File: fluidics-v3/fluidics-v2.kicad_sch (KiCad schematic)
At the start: 35 parts, among them J1 PJ-063AH, J10 87832-0410, J11 0705430001, J12 87832-0410, J13 0705430001, J14 87832-0410, J15 0533980671, J16 0705430001, J17 0533980671, J18 87832-0410, J19 0705430001, J2 B6B-ZR-SM4-TF, J20 0533980671, J21 87832-0410, J22 0705430001, J24 0705430001, J25 87832-0410, J3 A-DS_15_A_KG-T4S, J4 B6B-ZR-SM4-TF, U2 Teensy4.1

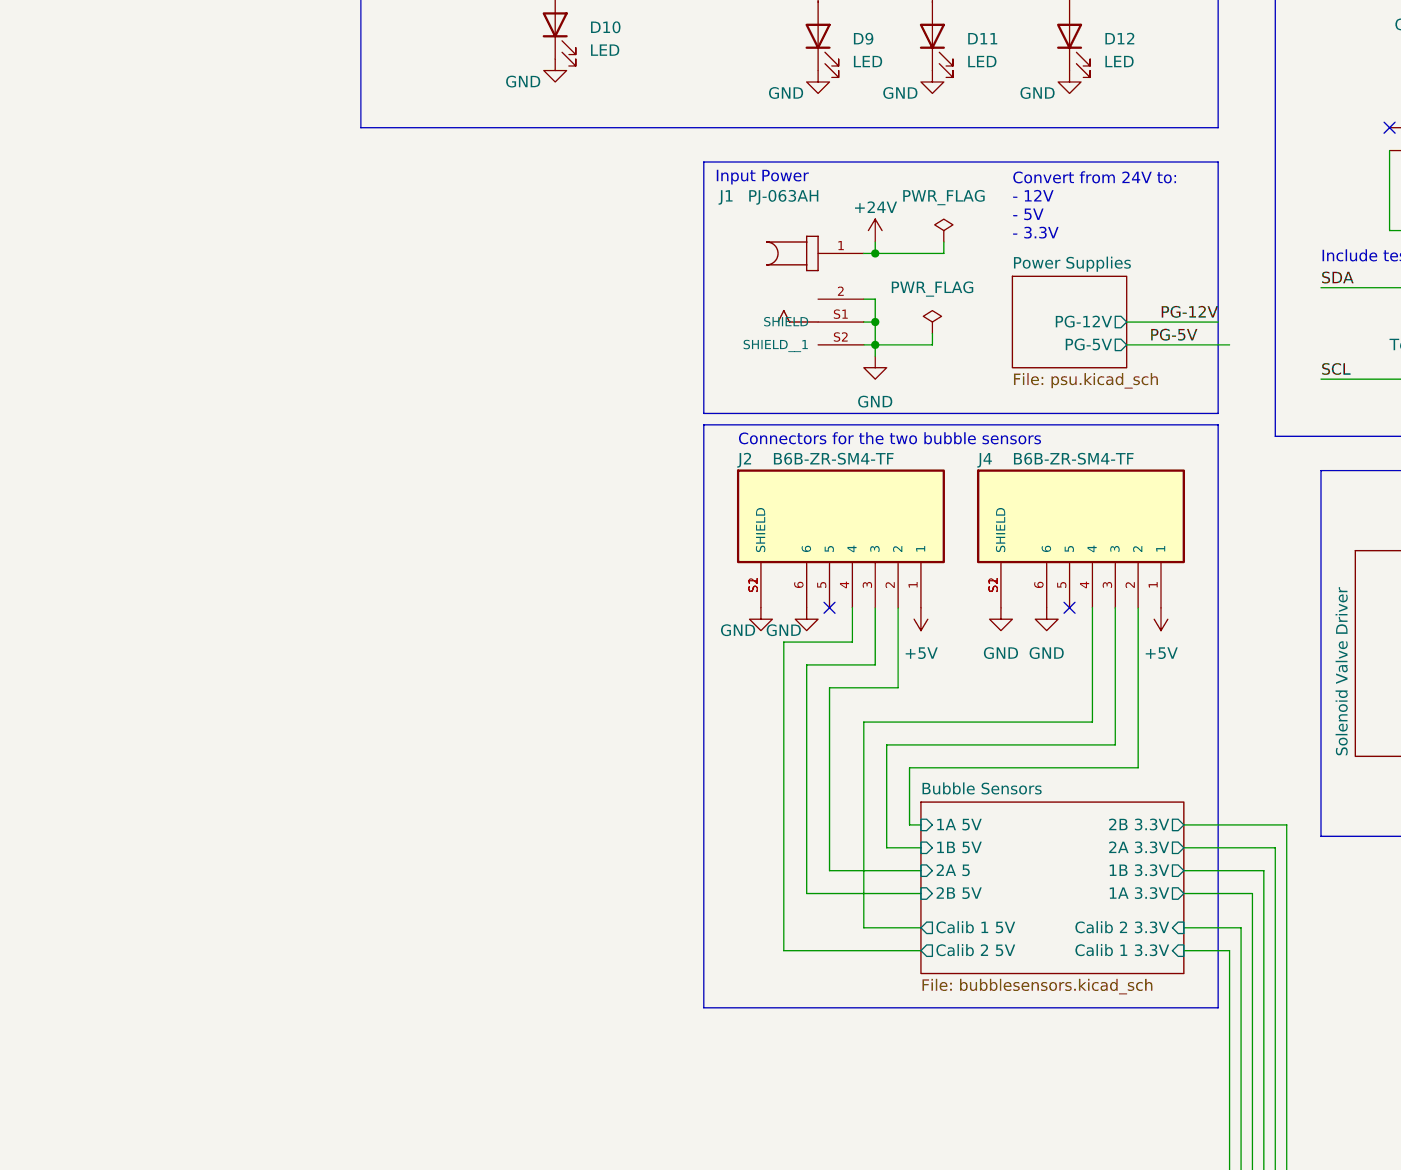
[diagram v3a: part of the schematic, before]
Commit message: v3 PCB: complete +24V input-protection front-end + downsize bulk caps
Input stage (J1 barrel jack -> TH1 NTC inrush limiter -> +24V plane):
- Fix +24V-into-J1 short + solder-mask bridge (leftover rail track ran
  into the /+24V_IN pad after J1 was repurposed as the input)
- Tie in U6.5 GND and C3 +24V bulk cap; stitch 3 isolated GND pour islands
- Route /+24V_IN on Front at 1.5mm (carries full board +24V current)

Bulk caps downsized, capacitance unchanged, all re-tied via-to-plane:
- C3  100uF/+24V: electrolytic CP_Elec_8x10.5 -> polymer CP_EIA-7343-20 (~2mm)
- C4   47uF/+3V3: electrolytic -> C_1206 ceramic
- C10 100uF/+5V:  electrolytic -> C_1210 ceramic
Schematic footprints updated to match (schematic/PCB parity clean).

DRC: 0 shorts/clearance/hole/isolated/parity; 6 unconnected
(5 intentional U2 no-connects + 1 pre-existing +5V stub gap).

Co-Authored-By: Claude Opus 4.8 (1M context) <noreply@anthropic.com>
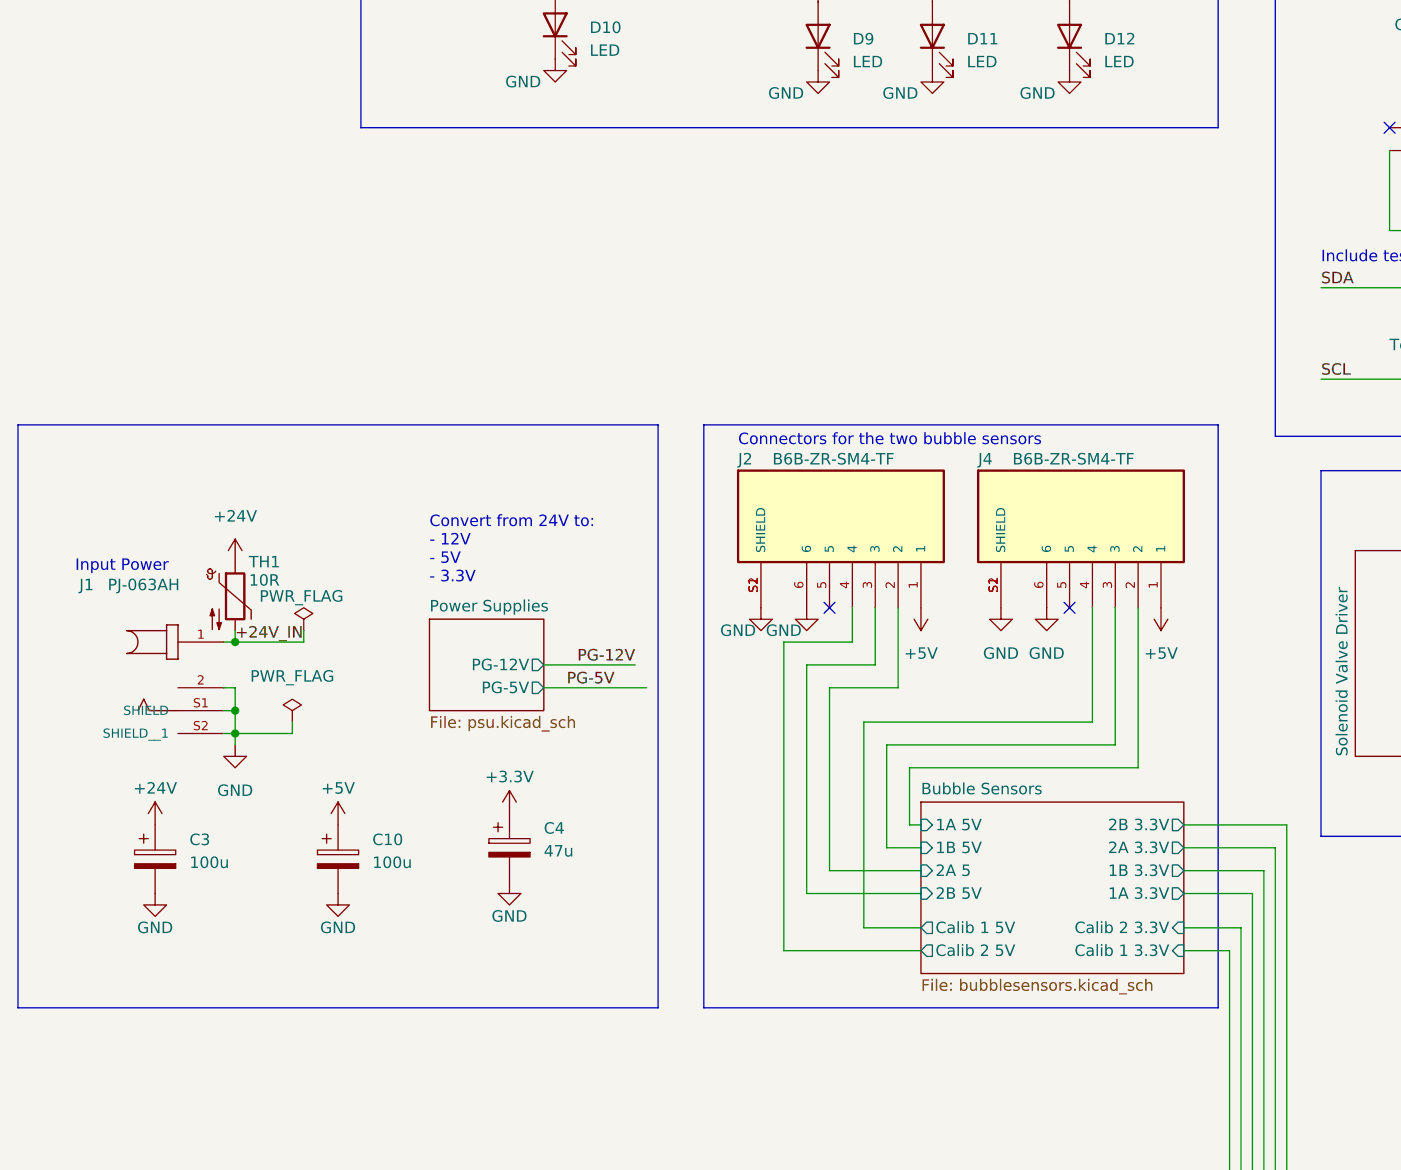
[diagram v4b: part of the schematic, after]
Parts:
- added C10: 100u, Capacitor_SMD:C_1210_3225Metric, symbol Device:C_Polarized
- added C3: 100u, Capacitor_Tantalum_SMD:CP_EIA-7343-20_Kemet-V, symbol Device:C_Polarized
- added C4: 47u, Capacitor_SMD:C_1206_3216Metric, symbol Device:C_Polarized
- added TH1: 10R, Varistor:RV_Disc_D7mm_W3.9mm_P5mm, symbol Device:Thermistor_NTC
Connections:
- net +24V: now also C3.1, TH1.1; no longer J1.1
- net +3.3V: now also C4.1
- net +5V: now also C10.1
- net GND: now also C10.2, C3.2, C4.2
- new net +24V_IN: J1.1, TH1.2
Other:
- moved on the sheet: J1

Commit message: v3: mounting holes M2->M3, relink C3/C4/C10, regen fab package
Mounting holes H2-H4: MountingHole_2.2mm_M2 -> 3.2mm_M3 (PCB + schematic,
parity clean). Note: still 3 holes, no H1 (the original board had 4x M3).

Fix bulk-cap schematic links. C3/C4/C10 had no (path) link to their
symbols and lacked the library prefix in their footprint id, so "Update
PCB from Schematic" deleted and re-added them (losing routing). Relinked:
- C3  Capacitor_Tantalum_SMD:CP_EIA-7343-20_Kemet-V -> /cbfc97bd
- C4  Capacitor_SMD:C_1206_3216Metric              -> /5064b71f
- C10 Capacitor_SMD:C_1210_3225Metric              -> /25d2ffd2

Regenerated fabrication/v3 (gerbers, drill incl. new 3.2mm tool, gerber
zip, STEP, BOM, positions) to reflect the M3 holes.

DRC: 0 clearance/hole/short/isolated, 0 schematic-parity. Remaining are
pre-existing: 24 malformed_courtyard on U2 (footprint geometry) and 6
unconnected (5 intentional U2 no-connects + 1 +5V stub).

Co-Authored-By: Claude Opus 4.8 (1M context) <noreply@anthropic.com>
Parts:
- H2, H3, H4: footprint MountingHole:MountingHole_2.2mm_M2_Pad_Via -> MountingHole:MountingHole_3.2mm_M3_Pad_Via
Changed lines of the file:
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@@
 			)
 		)
-		(property "Footprint" "MountingHole:MountingHole_2.2mm_M2_Pad_Via"
+		(property "Footprint" "MountingHole:MountingHole_3.2mm_M3_Pad_Via"
 			(at 199.39 261.62 0)
 			(hide yes)
@@
 			)
 		)
-		(property "Footprint" "MountingHole:MountingHole_2.2mm_M2_Pad_Via"
+		(property "Footprint" "MountingHole:MountingHole_3.2mm_M3_Pad_Via"
 			(at 203.2 266.7 0)
 			(hide yes)
@@
 			)
 		)
-		(property "Footprint" "MountingHole:MountingHole_2.2mm_M2_Pad_Via"
+		(property "Footprint" "MountingHole:MountingHole_3.2mm_M3_Pad_Via"
 			(at 199.39 279.4 0)
 			(hide yes)

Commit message: Split Teensy U2 into module + two 1x24 SMT sockets
U2 was one part standing in for three physical items: the Teensy 4.1 module
and the two 24-pin SMT socket strips it plugs into. The sockets existed only
as 3D models -- no refdes, no BOM line, no CPL entry -- so an assembler had
no way to order or place them.

New footprint teensy4.1:PinSocket_1x24_P2.54mm_Vertical_SMD_DualLand: 48 pads,
pin numbers 1-24 doubled, coordinates lifted verbatim from U2's lands. Every
pin has a land on both sides (the union of the Harwin M20-786 pin1-left and
pin1-right tail patterns), so strips fit in either orientation and a row may
be made up from shorter pieces. One footprint serves both sockets -- J7 is J6
rotated 180 degrees, which is why J7 pin n lands on old U2 pin n+24.

Schematic: J6/J7 (Conn_01x24) carry the 48 nets via labels on the root sheet;
GND power symbols on J6.1/J7.10/J7.23; no-connect flags on J6.2/J6.3/J6.15/
J7.22. U2 keeps its symbol and BOM line but is marked exclude-from-board.
Seven nets that had no root-sheet name were named to make the join explicit:
/Bubble Sensors/{2B,2A,1B,1A,Calib 2,Calib 1} 3.3V -> BUB_*, Net-(D21-K) -> VIN.

PCB: J6 at (170.61, 51.33) rot 0, J7 at (185.85, 51.33) rot 180 -- all 96 pads
sit exactly on the coordinates U2's lands occupied, so no copper moved. U2's
footprint removed. Module body added back as documentation: 61.0 x 17.78 mm
outline plus "U2 Teensy 4.1" on F.Fab, "U2 TEENSY 4.1" on F.Silkscreen in the
pad-free channel between the rows (no outline on silk -- the body edges cross
the socket lands, which is what generated the old silk_over_copper count).

Verified: 44/44 socket pins on the same net as their former U2 pin, 4/4
intended no-connects, 0 nets lost or created. DRC unconnected 6 (unchanged
baseline: 5 GPIO_8/9+SPI no-connects, 1 pre-existing +5V stub gap), schematic
parity 0, 0 electrical violations. Cosmetic violations 209 -> 85 (U2's
footprint took 24 malformed courtyards and ~96 silk_over_copper with it).
ERC introd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
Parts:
- added J6, J7: Socket_1x24_2.54mm_SMT, teensy4.1:PinSocket_1x24_P2.54mm_Vertical_SMD_DualLand, symbol Connector_Generic:Conn_01x24
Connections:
- net GND: now also J6.1 (Pin_1), J7.10 (Pin_10), J7.23 (Pin_23)
- net GPIO_1: now also J7.21 (Pin_21)
- net GPIO_2: now also J7.20 (Pin_20)
- net GPIO_3: now also J7.19 (Pin_19)
- net GPIO_4: now also J7.18 (Pin_18)
- net GPIO_5: now also J7.8 (Pin_8)
- net GPIO_6: now also J7.7 (Pin_7)
- net GPIO_7: now also J7.6 (Pin_6)
- net GPIO_8: now also J6.7 (Pin_7)
- net GPIO_9: now also J6.6 (Pin_6)
- net PG-12V: now also J6.24 (Pin_24)
- net PG-5V: now also J7.1 (Pin_1)
- net POT_ANALOG: now also J7.9 (Pin_9)
- net SCL: now also J7.16 (Pin_16)
- net SCL1: now also J7.14 (Pin_14)
- net SCL2: now also J6.16 (Pin_16)
- net SDA: now also J7.17 (Pin_17)
- net SDA1: now also J7.15 (Pin_15)
- net SDA2: now also J6.17 (Pin_17)
- net SPI_MISO: now also J6.14 (Pin_14)
- net SPI_MOSI: now also J6.13 (Pin_13)
- net SPI_SCK: now also J7.11 (Pin_11)
- net SPI_~{CS}_PRESS: now also J6.11 (Pin_11)
- net SPI_~{CS}_VALVES: now also J6.12 (Pin_12)
- net UART_RX_DISCPUMP: now also J7.12 (Pin_12)
- net UART_RX_SYRPUMP: now also J6.10 (Pin_10)
- net UART_TX_DISCPUMP: now also J7.13 (Pin_13)
- net UART_TX_SYRPUMP: now also J6.9 (Pin_9)
- net VALVES_PWM: now also J6.5 (Pin_5)
- net VALVES_~{RST}: now also J6.4 (Pin_4)
- net ~{CS}0: now also J7.5 (Pin_5)
- net ~{CS}1: now also J7.4 (Pin_4)
- net ~{CS}2: now also J7.3 (Pin_3)
- net ~{CS}3: now also J7.2 (Pin_2)
- net ~{INVALID}_SYRPUMP: now also J6.8 (Pin_8)
- net VIN: now reaches D21.1 (K), U2.48 (VIN)
- net VIN: now also J7.24 (Pin_24)
- net Bubble Sensors/1A 3.3V renamed BUB_1A
- net BUB_1A: now also J6.21 (Pin_21)
- net Bubble Sensors/1B 3.3V renamed BUB_1B
- net BUB_1B: now also J6.20 (Pin_20)
- net Bubble Sensors/2A 3.3V renamed BUB_2A
- net BUB_2A: now also J6.19 (Pin_19)
- net Bubble Sensors/2B 3.3V renamed BUB_2B
- net BUB_2B: now also J6.18 (Pin_18)
- net Bubble Sensors/Calib 1 3.3V renamed BUB_CALIB1
- net BUB_CALIB1: now also J6.23 (Pin_23)
- net Bubble Sensors/Calib 2 3.3V renamed BUB_CALIB2
- net BUB_CALIB2: now also J6.22 (Pin_22)
- no-connect marks 47 -> 51

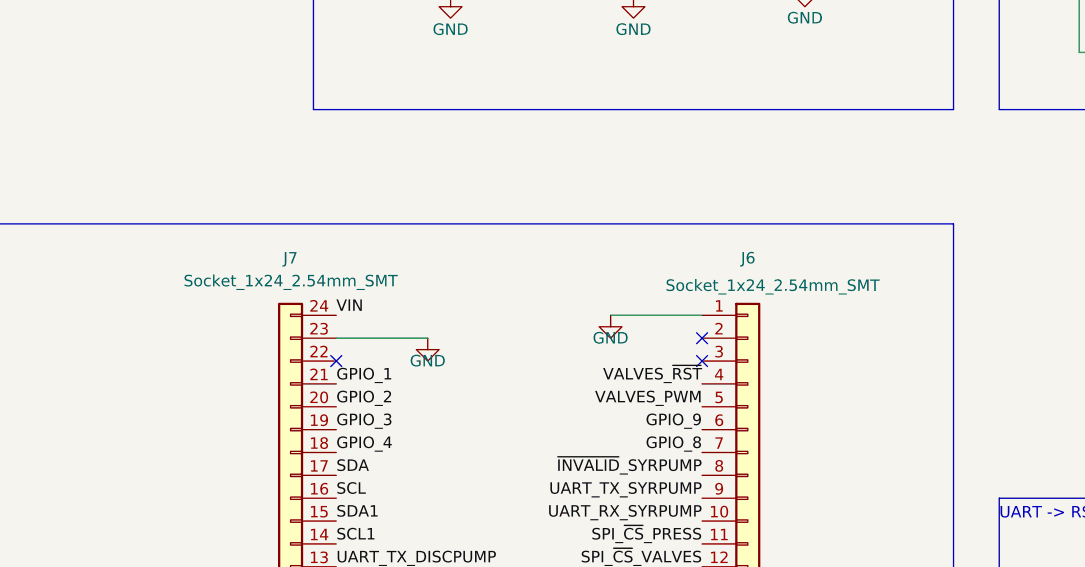
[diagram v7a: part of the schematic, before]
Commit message: Set socket MPN to Samtec SSM-124-L-SV
The land pattern was generated from Harwin's M20-786, but that series stops at
20 ways -- so no single Harwin part ever covered a row, and the board has never
had a one-part socket solution. Samtec's SSM-124-L-SV is a real 24-position
single-row 2.54mm SMT socket, and its footprint matches this land:

  tails         alternating          <- same
  offset        1.6025 mm            <- board has 1.65 mm, 47 um difference
  pad           1.905 x 1.02 mm      <- board has 1.9 x 1.0 mm
  pitch / span  2.54 / 58.42 mm      <- identical

Verified against the vendor footprint (SAMTEC_SSM-124-L-SV.kicad_mod). No
copper change: the tail sits 47 um off pad centre on a 1.9 mm pad. The
dual-land footprint is kept, so Harwin strips remain an alternative.

Value set on both the schematic and the board so BOM and CPL agree. Re-checked
after: 44/44 socket pins on the correct net, 4/4 intended no-connects, DRC
unconnected 6 (baseline), parity 0, 0 electrical violations. Fab package
regenerated.

Note: SSM-124-L-SV-P is the same socket with a pick-and-place pad, needed if
the sockets are to be machine placed rather than hand fitted. Only the plain
variant's land was verified here.

Co-Authored-By: Claude Opus 5 (1M context) <noreply@anthropic.com>
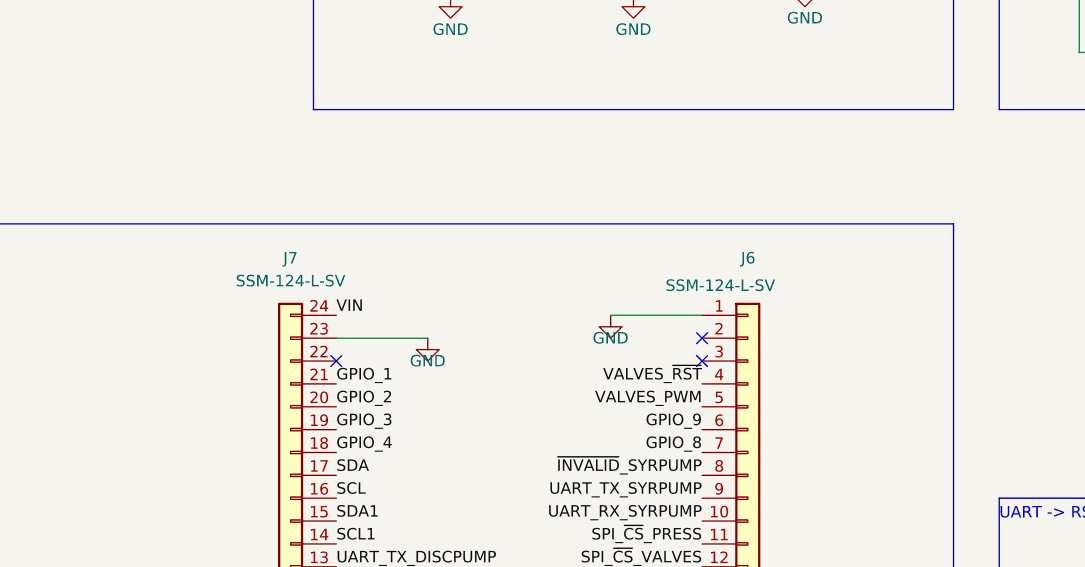
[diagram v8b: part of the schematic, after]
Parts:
- J6, J7: value Socket_1x24_2.54mm_SMT -> SSM-124-L-SV
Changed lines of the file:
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@@
 			)
 		)
-		(property "Value" "Socket_1x24_2.54mm_SMT"
+		(property "Value" "SSM-124-L-SV"
 			(at 97.536 210.058 0)
 			(show_name no)
@@
 			)
 		)
-		(property "Value" "Socket_1x24_2.54mm_SMT"
+		(property "Value" "SSM-124-L-SV"
 			(at 55.88 209.55 0)
 			(show_name no)
